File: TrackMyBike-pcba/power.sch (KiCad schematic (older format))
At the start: 34 parts

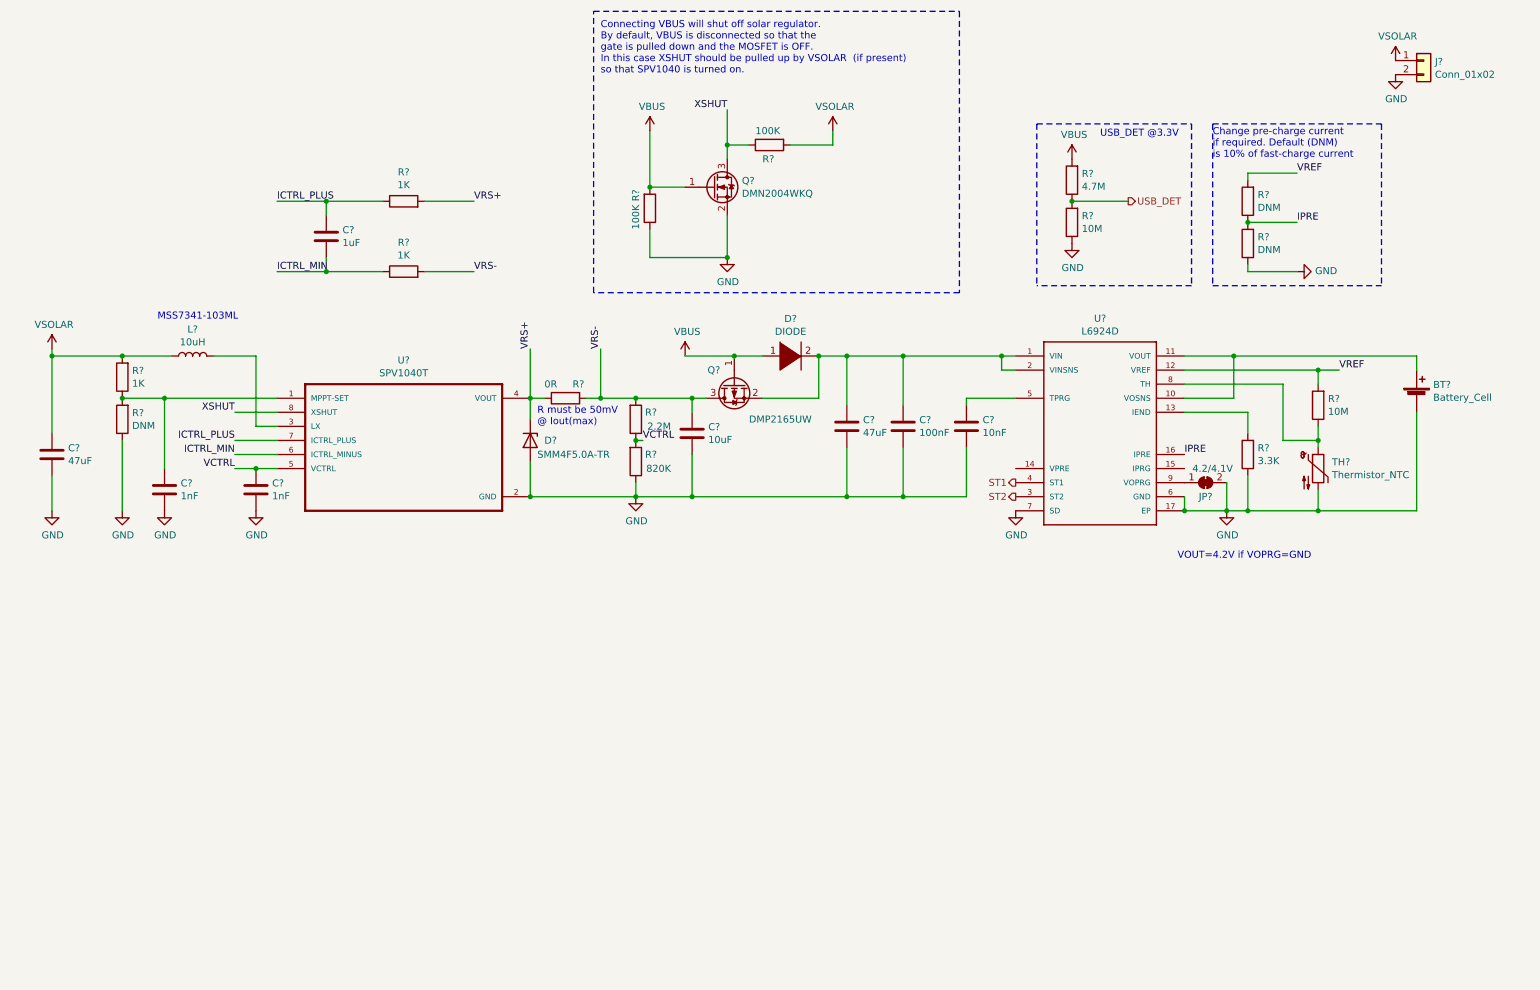
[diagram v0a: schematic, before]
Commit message: remove rescue files
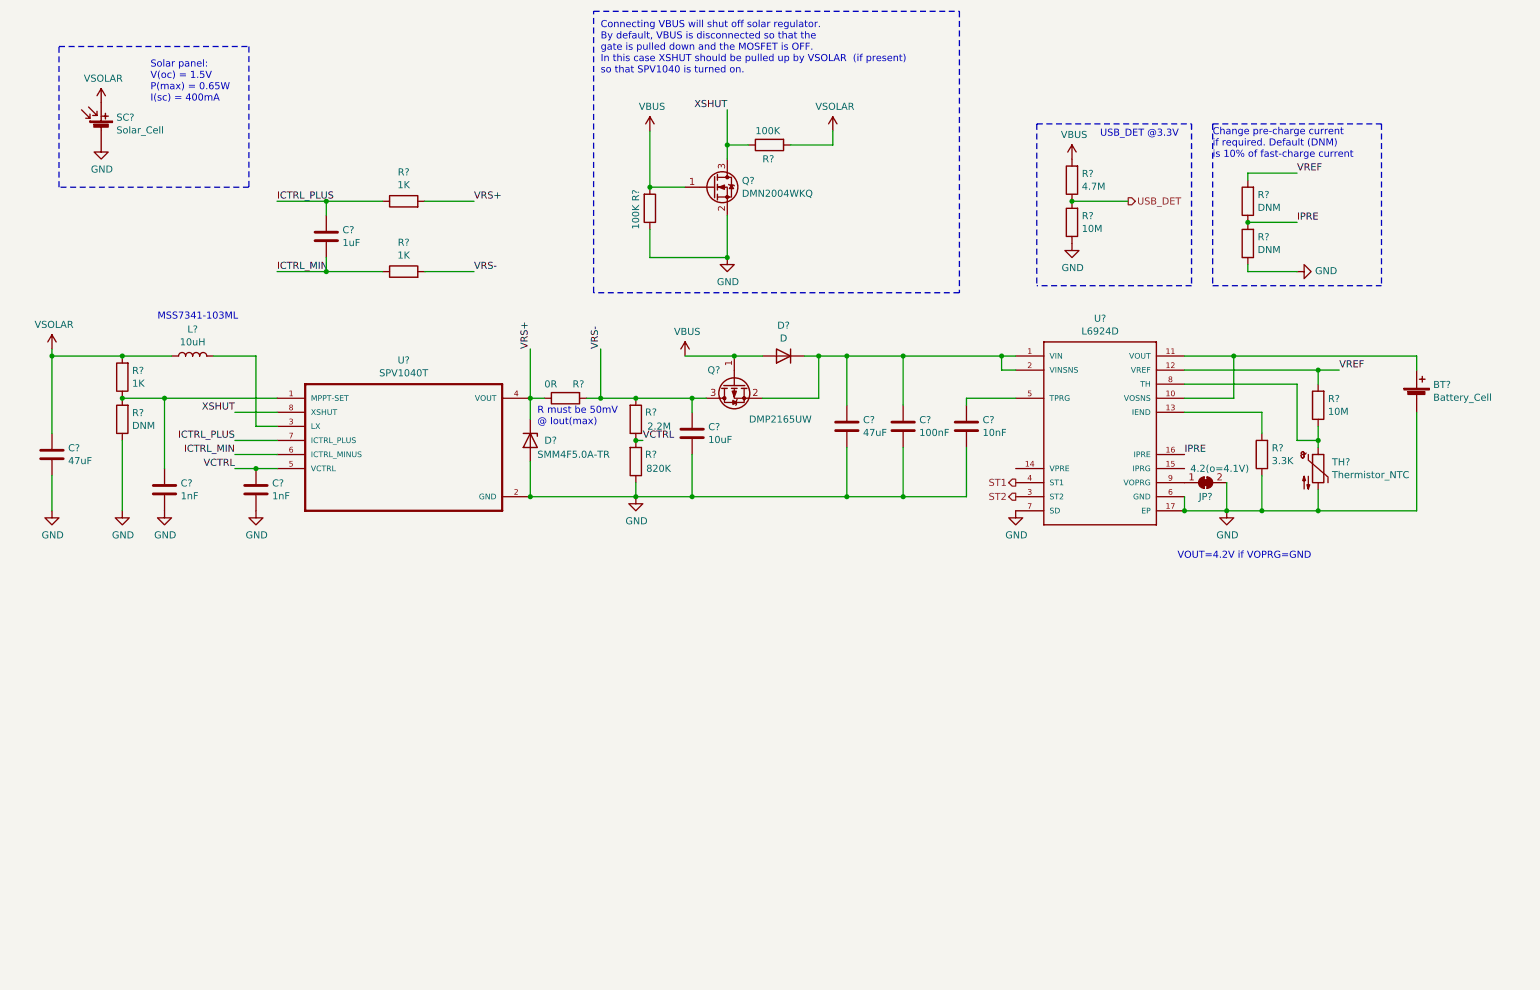
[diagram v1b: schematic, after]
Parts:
- removed D?: DIODE, symbol pspice:DIODE
- removed J?: Conn_01x02, symbol Connector_Generic:Conn_01x02
- added D?: D, symbol Device:D
- added SC?: Solar_Cell, symbol Device:Solar_Cell
- JP?: value 4.2/4.1V -> 4.2(o=4.1V)
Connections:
- net +1V0: now also SC?.1 (+)
- net GND: now also SC?.2 (-)
- net VBUS: now also D?.2 (A)
- net at C?.1, C?.1, Q?.2 (S)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: now also D?.1 (K)
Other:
- note added: "Solar panel:\nV(oc) = 1.5V\nP(max) = 0.65W\nI(sc) = 400mA"
- moved on the sheet: R?
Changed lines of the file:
@@
 U 1 1 5F1C0FA3
 P 3250 3700
+AR Path="/5F1C0FA3" Ref="U?"  Part="1"
+AR Path="/5F16A6AE/5F1C0FA3" Ref="U?"  Part="1"
 F 0 "U?" H 3250 4370 50  0000 C CNN
 F 1 "SPV1040T" H 3250 4279 50  0000 C CNN
@@
 U 1 1 5F1C2568
 P 8200 3500
+AR Path="/5F1C2568" Ref="U?"  Part="1"
+AR Path="/5F16A6AE/5F1C2568" Ref="U?"  Part="1"
 F 0 "U?" H 8200 4267 50  0000 C CNN
 F 1 "L6924D" H 8200 4176 50  0000 C CNN
@@
 F 3 "" H 9100 4100 50  0001 C CNN
 	1    9100 4100
-	1    0    0    -1
-$EndComp
-$Comp
-L pspice:DIODE D?
-U 1 1 5F1C4114
-P 6000 3000
-F 0 "D?" H 6000 3265 50  0000 C CNN
-F 1 "DIODE" H 6000 3174 50  0000 C CNN
-F 2 "" H 6000 3000 50  0001 C CNN
-F 3 "~" H 6000 3000 50  0001 C CNN
-	1    6000 3000
 	1    0    0    -1
 $EndComp
@@
 	9750 3950 9750 4100
 Wire Wire Line
-	9500 3200 9500 3600
-Wire Wire Line
-	9500 3600 9750 3600
-Wire Wire Line
-	8800 3200 9500 3200
+	9600 3200 9600 3600
+Wire Wire Line
+	9600 3600 9750 3600
+Wire Wire Line
+	8800 3200 9600 3200
 Connection ~ 9750 3600
 Wire Wire Line
@@
 Connection ~ 9100 4100
 Wire Wire Line
-	9100 4100 9250 4100
-$Comp
-L Connector_Generic:Conn_01x02 J?
-U 1 1 5F1E8D18
-P 10500 900
-AR Path="/5F1E8D18" Ref="J?"  Part="1"
-AR Path="/5F16A6AE/5F1E8D18" Ref="J?"  Part="1"
-F 0 "J?" H 10580 892 50  0000 L CNN
-F 1 "Conn_01x02" H 10580 801 50  0000 L CNN
-F 2 "" H 10500 900 50  0001 C CNN
-F 3 "~" H 10500 900 50  0001 C CNN
-	1    10500 900
-	1    0    0    -1
-$EndComp
+	9100 4100 9350 4100
 $Comp
 L power:GND #PWR?
 U 1 1 5F1E8D1E
-P 10300 1000
+P 1100 1500
 AR Path="/5F1E8D1E" Ref="#PWR?"  Part="1"
 AR Path="/5F16A6AE/5F1E8D1E" Ref="#PWR?"  Part="1"
-F 0 "#PWR?" H 10300 750 50  0001 C CNN
-F 1 "GND" H 10305 827 50  0000 C CNN
-F 2 "" H 10300 1000 50  0001 C CNN
-F 3 "" H 10300 1000 50  0001 C CNN
-	1    10300 1000
+F 0 "#PWR?" H 1100 1250 50  0001 C CNN
+F 1 "GND" H 1105 1327 50  0000 C CNN
+F 2 "" H 1100 1500 50  0001 C CNN
+F 3 "" H 1100 1500 50  0001 C CNN
+	1    1100 1500
 	1    0    0    -1
 $EndComp
@@
 L power:VSOLAR #PWR?
 U 1 1 5F1E8D24
-P 10300 900
+P 1100 1200
 AR Path="/5F1E8D24" Ref="#PWR?"  Part="1"
 AR Path="/5F16A6AE/5F1E8D24" Ref="#PWR?"  Part="1"
-F 0 "#PWR?" H 10300 750 50  0001 C CNN
-F 1 "VSOLAR" H 10315 1073 50  0000 C CNN
-F 2 "" H 10300 900 50  0001 C CNN
-F 3 "" H 10300 900 50  0001 C CNN
-	1    10300 900
+F 0 "#PWR?" H 1100 1050 50  0001 C CNN
+F 1 "VSOLAR" H 1115 1373 50  0000 C CNN
+F 2 "" H 1100 1200 50  0001 C CNN
+F 3 "" H 1100 1200 50  0001 C CNN
+	1    1100 1200
 	1    0    0    -1
 $EndComp
@@
 P 8950 3900
 F 0 "JP?" H 8950 3800 50  0000 C CNN
-F 1 "4.2/4.1V" H 9000 4000 50  0000 C CNN
+F 1 "4.2(o=4.1V)" H 9050 4000 50  0000 C CNN
 F 2 "" H 8950 3900 50  0001 C CNN
 F 3 "~" H 8950 3900 50  0001 C CNN
@@
 Text Notes 1500 2750 0    50   ~ 0
 MSS7341-103ML
-Connection ~ 6200 3000
 $Comp
 L Device:C C?
@@
 L Device:R R?
 U 1 1 5F3C2354
-P 9250 3700
-F 0 "R?" H 9180 3654 50  0000 R CNN
-F 1 "3.3K" H 9180 3745 50  0000 R CNN
-F 2 "" V 9180 3700 50  0001 C CNN
-F 3 "~" H 9250 3700 50  0001 C CNN
-	1    9250 3700
+P 9350 3700
+F 0 "R?" H 9280 3654 50  0000 R CNN
+F 1 "3.3K" H 9280 3745 50  0000 R CNN
+F 2 "" V 9280 3700 50  0001 C CNN
+F 3 "~" H 9350 3700 50  0001 C CNN
+	1    9350 3700
 	-1   0    0    1
 $EndComp
 Wire Wire Line
-	8800 3400 9250 3400
-Wire Wire Line
-	9250 3850 9250 4100
-Connection ~ 9250 4100
-Wire Wire Line
-	9250 4100 9750 4100
-Wire Wire Line
-	9250 3400 9250 3550
+	9350 3850 9350 4100
+Connection ~ 9350 4100
+Wire Wire Line
+	9350 4100 9750 4100
+Wire Wire Line
+	9350 3400 9350 3550
 Text Label 8800 3700 0    50   ~ 0
 IPRE
@@
 Wire Notes Line
 	9000 2500 10200 2500
+$Comp
+L Device:D D?
+U 1 1 5F23C2ED
+P 5950 3000
+F 0 "D?" H 5950 2783 50  0000 C CNN
+F 1 "D" H 5950 2874 50  0000 C CNN
+F 2 "" H 5950 3000 50  0001 C CNN
+F 3 "~" H 5950 3000 50  0001 C CNN
+	1    5950 3000
+	-1   0    0    1
+$EndComp
+Wire Wire Line
+	6100 3000 6200 3000
+Connection ~ 6200 3000
+Wire Wire Line
+	8800 3400 9350 3400
+$Comp
+L Device:Solar_Cell SC?
+U 1 1 5F259849
+P 1100 1400
+F 0 "SC?" H 1208 1496 50  0000 L CNN
+F 1 "Solar_Cell" H 1208 1405 50  0000 L CNN
+F 2 "" V 1100 1460 50  0001 C CNN
+F 3 "~" V 1100 1460 50  0001 C CNN
+	1    1100 1400
+	1    0    0    -1
+$EndComp
+Text Notes 1450 1200 0    50   ~ 0
+Solar panel:\nV(oc) = 1.5V\nP(max) = 0.65W\nI(sc) = 400mA
+Wire Notes Line
+	2150 800  2150 1800
+Wire Notes Line
+	2150 1800 800  1800
+Wire Notes Line
+	800  1800 800  800
+Wire Notes Line
+	800  800  2150 800
 $EndSCHEMATC

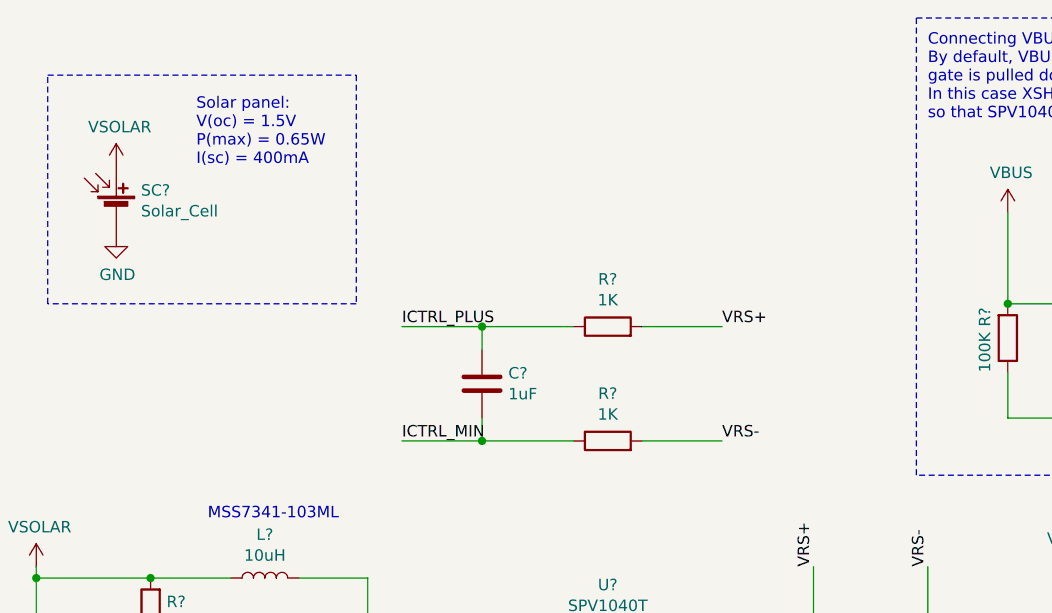
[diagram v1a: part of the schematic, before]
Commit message: Add powersupply battery charger circuit
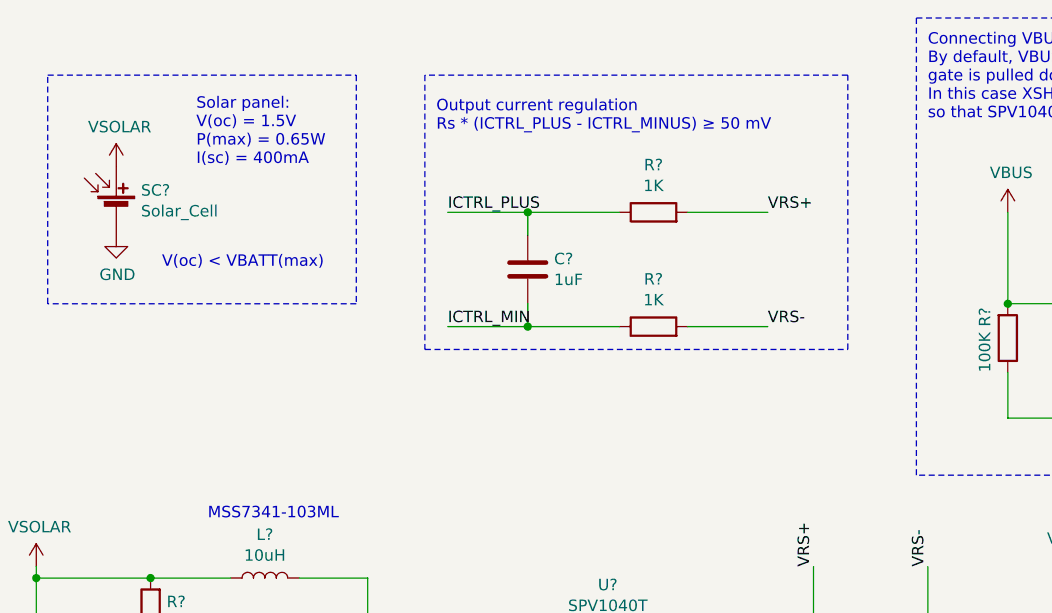
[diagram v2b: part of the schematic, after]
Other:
- note added: "Output current regulation \nRs * (ICTRL_PLUS - ICTRL_MINUS) ≥ 50 mV"
- note added: "V(oc) < VBATT(max)"
- moved on the sheet: C?, R?
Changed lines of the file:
@@
 L Device:C C?
 U 1 1 5F203267
-P 2700 2150
-F 0 "C?" H 2815 2196 50  0000 L CNN
-F 1 "1uF" H 2815 2105 50  0000 L CNN
-F 2 "" H 2738 2000 50  0001 C CNN
-F 3 "~" H 2700 2150 50  0001 C CNN
-	1    2700 2150
+P 2900 1650
+F 0 "C?" H 3015 1696 50  0000 L CNN
+F 1 "1uF" H 3015 1605 50  0000 L CNN
+F 2 "" H 2938 1500 50  0001 C CNN
+F 3 "~" H 2900 1650 50  0001 C CNN
+	1    2900 1650
 	1    0    0    -1
 $EndComp
@@
 L Device:R R?
 U 1 1 5F2038E9
-P 3250 1900
-F 0 "R?" V 3457 1900 50  0000 C CNN
-F 1 "1K" V 3366 1900 50  0000 C CNN
-F 2 "" V 3180 1900 50  0001 C CNN
-F 3 "~" H 3250 1900 50  0001 C CNN
-	1    3250 1900
+P 3450 1400
+F 0 "R?" V 3657 1400 50  0000 C CNN
+F 1 "1K" V 3566 1400 50  0000 C CNN
+F 2 "" V 3380 1400 50  0001 C CNN
+F 3 "~" H 3450 1400 50  0001 C CNN
+	1    3450 1400
 	0    -1   -1   0
 $EndComp
@@
 L Device:R R?
 U 1 1 5F203FF2
-P 3250 2400
-F 0 "R?" V 3457 2400 50  0000 C CNN
-F 1 "1K" V 3366 2400 50  0000 C CNN
-F 2 "" V 3180 2400 50  0001 C CNN
-F 3 "~" H 3250 2400 50  0001 C CNN
-	1    3250 2400
+P 3450 1900
+F 0 "R?" V 3657 1900 50  0000 C CNN
+F 1 "1K" V 3566 1900 50  0000 C CNN
+F 2 "" V 3380 1900 50  0001 C CNN
+F 3 "~" H 3450 1900 50  0001 C CNN
+	1    3450 1900
 	0    -1   -1   0
 $EndComp
 Wire Wire Line
-	3100 1900 2700 1900
-Wire Wire Line
-	2700 1900 2700 2000
-Wire Wire Line
-	2700 2300 2700 2400
-Wire Wire Line
-	2700 2400 3100 2400
-Wire Wire Line
-	2700 1900 2350 1900
-Connection ~ 2700 1900
-Wire Wire Line
-	2700 2400 2350 2400
-Connection ~ 2700 2400
-Wire Wire Line
-	3400 2400 3750 2400
-Wire Wire Line
-	3400 1900 3750 1900
-Text Label 3750 2400 0    50   ~ 0
+	3300 1400 2900 1400
+Wire Wire Line
+	2900 1400 2900 1500
+Wire Wire Line
+	2900 1800 2900 1900
+Wire Wire Line
+	2900 1900 3300 1900
+Wire Wire Line
+	2900 1400 2550 1400
+Connection ~ 2900 1400
+Wire Wire Line
+	2900 1900 2550 1900
+Connection ~ 2900 1900
+Wire Wire Line
+	3600 1900 3950 1900
+Wire Wire Line
+	3600 1400 3950 1400
+Text Label 3950 1900 0    50   ~ 0
 VRS-
-Text Label 3750 1900 0    50   ~ 0
+Text Label 3950 1400 0    50   ~ 0
 VRS+
-Text Label 2350 1900 0    50   ~ 0
+Text Label 2550 1400 0    50   ~ 0
 ICTRL_PLUS
-Text Label 2350 2400 0    50   ~ 0
+Text Label 2550 1900 0    50   ~ 0
 ICTRL_MIN
 Text Label 2050 3600 2    50   ~ 0
@@
 Wire Notes Line
 	800  800  2150 800
+Text Notes 2500 1050 0    50   ~ 0
+Output current regulation \nRs * (ICTRL_PLUS - ICTRL_MINUS) ≥ 50 mV
+Wire Notes Line
+	2450 2000 4300 2000
+Wire Notes Line
+	4300 2000 4300 800
+Wire Notes Line
+	4300 800  2450 800
+Wire Notes Line
+	2450 800  2450 2000
+Text Notes 1300 1650 0    50   ~ 0
+V(oc) < VBATT(max)
 $EndSCHEMATC
